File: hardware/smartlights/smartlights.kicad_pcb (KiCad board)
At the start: 2 copper layers, 40 x 65 mm, 22 parts, among them J1 Conn_02x20_Odd_Even_MountingP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, J10 Conn_01x02_MountingPin, J11 Conn_01x02_MountingPin, J2 Conn_01x02_MountingPin, J3 Conn_Coaxial_Power, J4 Conn_01x02_MountingPin, J5 Conn_01x04, J6 Conn_01x02_MountingPin, J7 Conn_01x02_MountingPin, J8 Conn_01x02_MountingPin, J9 Conn_01x02_MountingPin, Q1 IRLZ34N, Q2 IRLZ34N, Q3 IRLZ34N, Q4 IRLZ34N, Q5 IRLZ34N, Q6 IRLZ34N, U1 LM2596T-5

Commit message: Neaten up labels, GND area
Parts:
- renumbered J2 to J1, J3 to J10, J1 to J11, J5 to J2, J6 to J3, J9 to J5, J8 to J6, J11 to J8, J10 to J9
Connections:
- J5 pad 2: Net-(J1-Pad20) -> GND
- J6 pad 2: Net-(J1-Pad20) -> GND
- J7 pad 2: Net-(J1-Pad20) -> GND
- J8 pad 2: Net-(J1-Pad20) -> GND
- J9 pad 2: Net-(J1-Pad20) -> GND
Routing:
- net Net-(J1-Pad20): track 39.5 -> 0.00 mm
- net Net-(J1-Pad22): track 0.00 -> 6.51 mm
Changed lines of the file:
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@@
   (general
     (thickness 1.6)
-    (drawings 14)
-    (tracks 139)
+    (drawings 17)
+    (tracks 132)
     (zones 0)
     (modules 22)
@@
     (descr "Through hole straight pin header, 1x02, 2.54mm pitch, single row")
     (tags "Through hole pin header THT 1x02 2.54mm single row")
-    (fp_text reference J11 (at 0 -2.33 90) (layer F.SilkS)
+    (fp_text reference J8 (at 2.54 2.54 180) (layer F.SilkS)
       (effects (font (size 1 1) (thickness 0.15)))
     )
@@
     (fp_line (start -0.635 -1.27) (end 1.27 -1.27) (layer F.Fab) (width 0.1))
     (pad 2 thru_hole oval (at 0 2.54 90) (size 1.7 1.7) (drill 1) (layers *.Cu *.Mask)
-      (net 20 "Net-(J1-Pad20)"))
+      (net 1 GND))
     (pad 1 thru_hole rect (at 0 0 90) (size 1.7 1.7) (drill 1) (layers *.Cu *.Mask)
       (net 17 "Net-(J1-Pad24)"))
@@
     (descr "Through hole straight pin header, 1x02, 2.54mm pitch, single row")
     (tags "Through hole pin header THT 1x02 2.54mm single row")
-    (fp_text reference J10 (at 0 -2.33 90) (layer F.SilkS)
+    (fp_text reference J9 (at 2.54 2.54 180) (layer F.SilkS)
       (effects (font (size 1 1) (thickness 0.15)))
     )
@@
     (fp_line (start -0.635 -1.27) (end 1.27 -1.27) (layer F.Fab) (width 0.1))
     (pad 2 thru_hole oval (at 0 2.54 90) (size 1.7 1.7) (drill 1) (layers *.Cu *.Mask)
-      (net 20 "Net-(J1-Pad20)"))
+      (net 1 GND))
     (pad 1 thru_hole rect (at 0 0 90) (size 1.7 1.7) (drill 1) (layers *.Cu *.Mask)
       (net 16 "Net-(J1-Pad26)"))
@@
     (descr "Through hole straight pin header, 1x02, 2.54mm pitch, single row")
     (tags "Through hole pin header THT 1x02 2.54mm single row")
-    (fp_text reference J9 (at 0 -2.33 90) (layer F.SilkS)
+    (fp_text reference J5 (at 2.54 2.54 180) (layer F.SilkS)
       (effects (font (size 1 1) (thickness 0.15)))
     )
@@
     (fp_line (start -0.635 -1.27) (end 1.27 -1.27) (layer F.Fab) (width 0.1))
     (pad 2 thru_hole oval (at 0 2.54 90) (size 1.7 1.7) (drill 1) (layers *.Cu *.Mask)
-      (net 20 "Net-(J1-Pad20)"))
+      (net 1 GND))
     (pad 1 thru_hole rect (at 0 0 90) (size 1.7 1.7) (drill 1) (layers *.Cu *.Mask)
       (net 23 "Net-(J1-Pad16)"))
@@
     (descr "Through hole straight pin header, 1x02, 2.54mm pitch, single row")
     (tags "Through hole pin header THT 1x02 2.54mm single row")
-    (fp_text reference J8 (at 0 -2.33 90) (layer F.SilkS)
+    (fp_text reference J6 (at 2.54 2.54 180) (layer F.SilkS)
       (effects (font (size 1 1) (thickness 0.15)))
     )
@@
     (fp_line (start -0.635 -1.27) (end 1.27 -1.27) (layer F.Fab) (width 0.1))
     (pad 2 thru_hole oval (at 0 2.54 90) (size 1.7 1.7) (drill 1) (layers *.Cu *.Mask)
-      (net 20 "Net-(J1-Pad20)"))
+      (net 1 GND))
     (pad 1 thru_hole rect (at 0 0 90) (size 1.7 1.7) (drill 1) (layers *.Cu *.Mask)
       (net 21 "Net-(J1-Pad18)"))
@@
     (descr "Through hole straight pin header, 1x02, 2.54mm pitch, single row")
     (tags "Through hole pin header THT 1x02 2.54mm single row")
-    (fp_text reference J7 (at 0 -2.33 90) (layer F.SilkS)
+    (fp_text reference J7 (at 2.54 2.54 180) (layer F.SilkS)
       (effects (font (size 1 1) (thickness 0.15)))
     )
@@
     (fp_line (start -0.635 -1.27) (end 1.27 -1.27) (layer F.Fab) (width 0.1))
     (pad 2 thru_hole oval (at 0 2.54 90) (size 1.7 1.7) (drill 1) (layers *.Cu *.Mask)
-      (net 20 "Net-(J1-Pad20)"))
+      (net 1 GND))
     (pad 1 thru_hole rect (at 0 0 90) (size 1.7 1.7) (drill 1) (layers *.Cu *.Mask)
       (net 19 "Net-(J1-Pad22)"))
@@
     (descr "TO-220-3, Vertical, RM 2.54mm, see https://www.vishay.com/docs/66542/to-220-1.pdf")
     (tags "TO-220-3 Vertical RM 2.54mm")
-    (fp_text reference Q5 (at 2 2.5 90) (layer F.SilkS)
+    (fp_text reference Q5 (at 2 2.5 180) (layer F.SilkS)
       (effects (font (size 1 1) (thickness 0.15)))
     )
@@
     (descr "Through hole straight pin header, 1x02, 2.54mm pitch, single row")
     (tags "Through hole pin header THT 1x02 2.54mm single row")
-    (fp_text reference J6 (at 0 -2.33) (layer F.SilkS)
+    (fp_text reference J3 (at 0 -2.33) (layer F.SilkS)
       (effects (font (size 1 1) (thickness 0.15)))
     )
@@
     (descr "Through hole straight pin header, 1x04, 2.54mm pitch, single row")
     (tags "Through hole pin header THT 1x04 2.54mm single row")
-    (fp_text reference J5 (at 0 -2.33) (layer F.SilkS)
+    (fp_text reference J2 (at 0 -2.33) (layer F.SilkS)
       (effects (font (size 1 1) (thickness 0.15)))
     )
@@
     (descr "Diode, DO-201AD series, Axial, Horizontal, pin pitch=15.24mm, , length*diameter=9.5*5.2mm^2, , http://www.diodes.com/_files/packages/DO-201AD.pdf")
     (tags "Diode DO-201AD series Axial Horizontal pin pitch 15.24mm  length 9.5mm diameter 5.2mm")
-    (fp_text reference D1 (at 14 2.5 90) (layer F.SilkS)
+    (fp_text reference D1 (at 13.65 3.19 180) (layer F.SilkS)
       (effects (font (size 1 1) (thickness 0.15)))
     )
@@
       (effects (font (size 1 1) (thickness 0.15)))
     )
-    (fp_text user K (at 0.5 3 90) (layer F.SilkS)
+    (fp_text user K (at 0.5 3 180) (layer F.SilkS)
       (effects (font (size 1 1) (thickness 0.15)))
     )
@@
     (descr "TO-220-5, Vertical, RM 1.7mm, Pentawatt, Multiwatt-5, staggered type-1, see http://www.analog.com/media/en/package-pcb-resources/package/pkg_pdf/ltc-legacy-to-220/to-220_5_05-08-1421.pdf?domain=www.linear.com, https://www.diodes.com/assets/Package-Files/TO220-5.pdf")
     (tags "TO-220-5 Vertical RM 1.7mm Pentawatt Multiwatt-5 staggered type-1")
-    (fp_text reference U1 (at 3.4 -9.32 90) (layer F.SilkS)
+    (fp_text reference U1 (at 9.84 -7.42 180) (layer F.SilkS)
       (effects (font (size 1 1) (thickness 0.15)))
     )
@@
     (descr "DC Barrel Jack")
     (tags "Power Jack")
-    (fp_text reference J3 (at -8.45 5.75 90) (layer F.SilkS)
+    (fp_text reference J10 (at -7.88 6.59 180) (layer F.SilkS)
       (effects (font (size 1 1) (thickness 0.15)))
     )
@@
     (descr "Through hole straight pin header, 1x02, 2.54mm pitch, single row")
     (tags "Through hole pin header THT 1x02 2.54mm single row")
-    (fp_text reference J2 (at 0 -2.33) (layer F.SilkS)
+    (fp_text reference J1 (at 0 -2.33) (layer F.SilkS)
       (effects (font (size 1 1) (thickness 0.15)))
     )
@@
     (descr "Through hole straight socket strip, 2x20, 2.54mm pitch, double cols (from Kicad 4.0.7), script generated")
     (tags "Through hole socket strip THT 2x20 2.54mm double row")
-    (fp_text reference J1 (at -1.27 2.77) (layer B.SilkS)
+    (fp_text reference J11 (at 1.23 2.77) (layer B.SilkS)
       (effects (font (size 1 1) (thickness 0.15)) (justify mirror))
     )
@@
     )
   )
+  (gr_line (start 130 68) (end 130 127) (layer B.SilkS) (width 0.12))
+  (gr_arc (start 127 68) (end 130 68) (angle -90) (layer B.SilkS) (width 0.12))
+  (gr_arc (start 127 127) (end 127 130) (angle -90) (layer B.SilkS) (width 0.12))
   (gr_text "rev. 2.1" (at 108.5 128) (layer F.SilkS)
     (effects (font (size 1 1) (thickness 0.15)))
   )
-  (gr_text github.com/mrwonko/smartlights (at 104 87 270) (layer B.SilkS)
+  (gr_text github.com/mrwonko/smartlights (at 138 97 90) (layer B.SilkS)
     (effects (font (size 1 1) (thickness 0.15)) (justify mirror))
   )
@@
   (segment (start 133.35 103.04) (end 131.62 101.31) (width 0.25) (layer F.Cu) (net 17))
   (segment (start 133.35 104.14) (end 133.35 103.04) (width 0.25) (layer F.Cu) (net 17))
-  (segment (start 134.664999 95.294999) (end 135.040001 95.670001) (width 0.25) (layer F.Cu) (net 20))
-  (segment (start 135.040001 95.670001) (end 135.89 96.52) (width 0.25) (layer F.Cu) (net 20))
-  (segment (start 129.907082 95.294999) (end 134.664999 95.294999) (width 0.25) (layer F.Cu) (net 20))
-  (segment (start 128.972081 96.23) (end 129.907082 95.294999) (width 0.25) (layer F.Cu) (net 20))
-  (segment (start 127.77 96.23) (end 128.972081 96.23) (width 0.25) (layer F.Cu) (net 20))
-  (segment (start 135.89 81.28) (end 135.89 88.9) (width 0.25) (layer F.Cu) (net 20))
-  (segment (start 135.89 88.9) (end 135.89 96.52) (width 0.25) (layer F.Cu) (net 20))
-  (segment (start 135.89 96.52) (end 135.89 104.14) (width 0.25) (layer F.Cu) (net 20))
-  (segment (start 135.89 104.14) (end 135.89 111.76) (width 0.25) (layer F.Cu) (net 20))
+  (segment (start 130.02 96.52) (end 127.77 98.77) (width 0.25) (layer F.Cu) (net 19))
+  (segment (start 133.35 96.52) (end 130.02 96.52) (width 0.25) (layer F.Cu) (net 19))
   (segment (start 132.56 88.9) (end 133.35 88.9) (width 0.25) (layer F.Cu) (net 21))
   (segment (start 127.77 93.69) (end 132.56 88.9) (width 0.25) (layer F.Cu) (net 21))
@@
     (polygon
       (pts
-        (xy 124 102.5) (xy 116 110.5) (xy 116 115) (xy 111.5 119.5) (xy 106 119.5)
-        (xy 106 102.5) (xy 101 102.5) (xy 101 71.5) (xy 106.5 71.5) (xy 106.5 66)
-        (xy 124 66)
+        (xy 140 130) (xy 100 130) (xy 100 65) (xy 140 65)
       )
     )

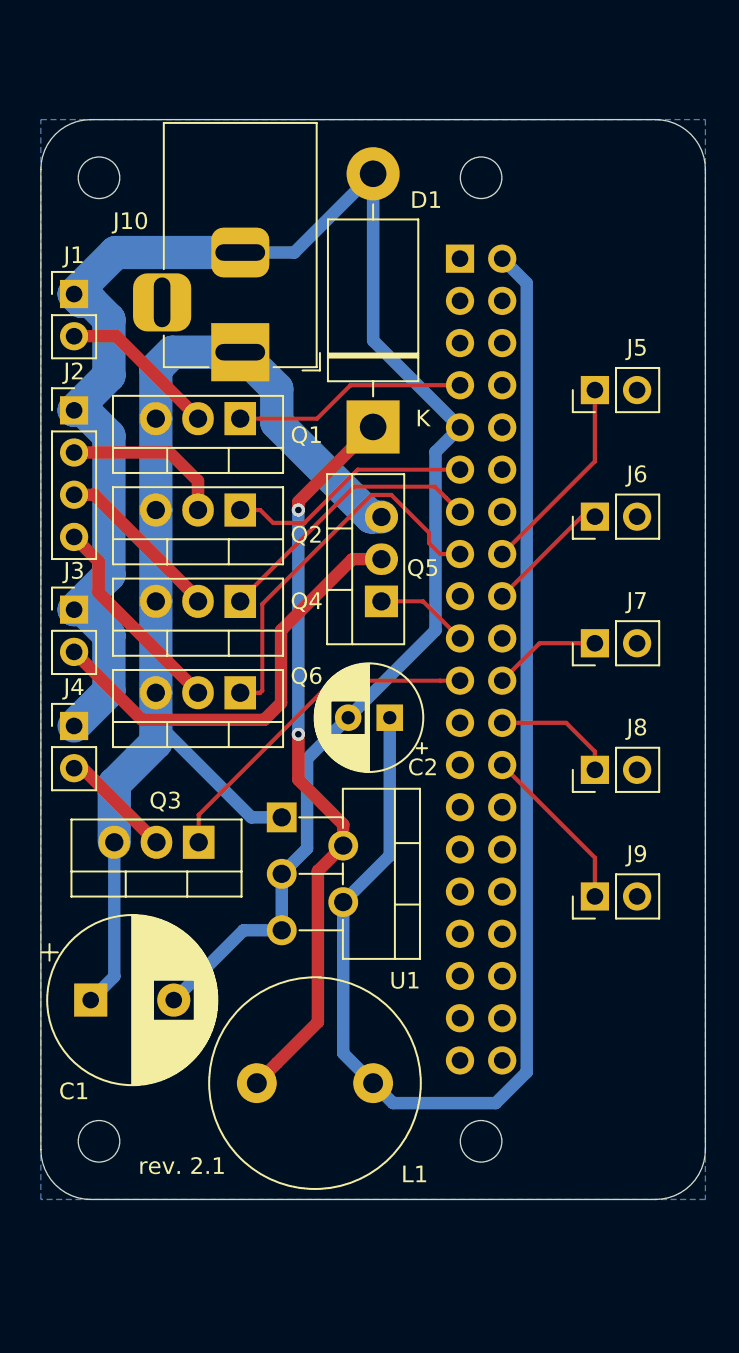
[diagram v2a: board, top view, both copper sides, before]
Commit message: PCB: Use RasPi footprint, reduce GND area around jacks
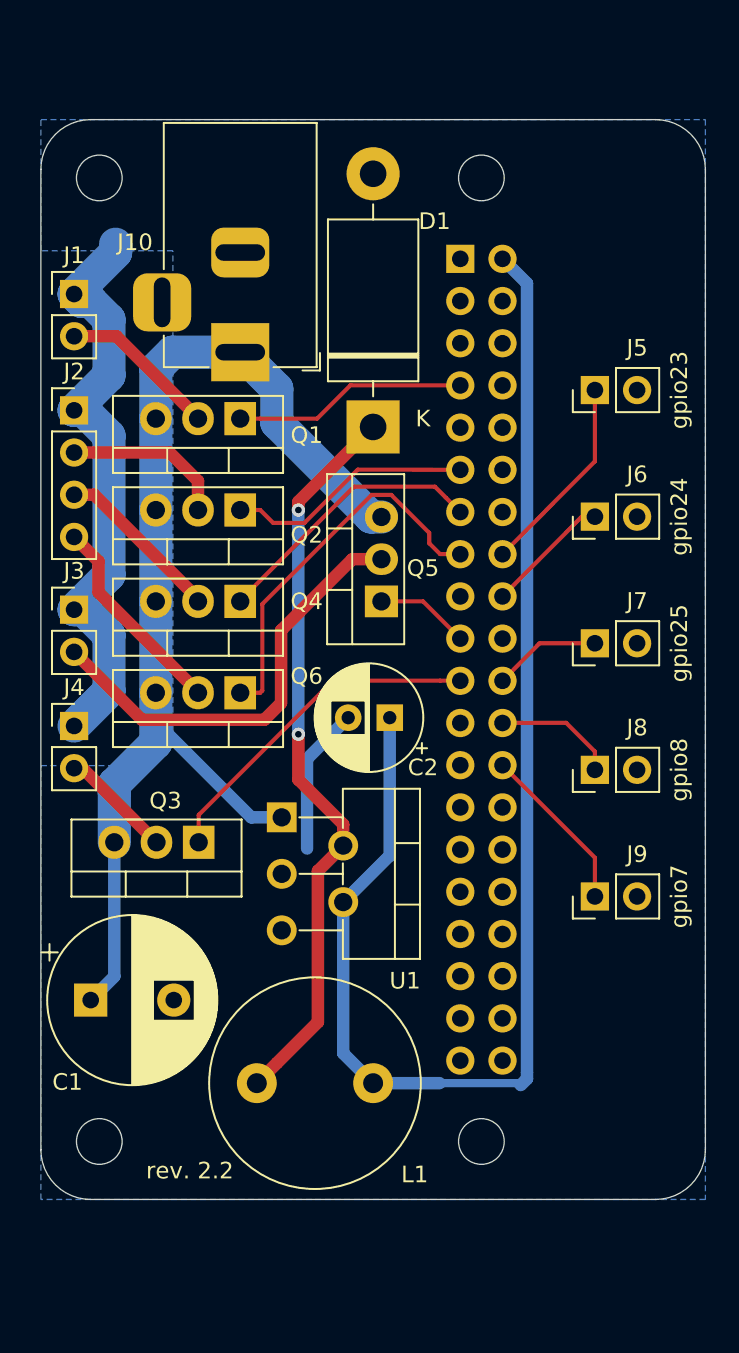
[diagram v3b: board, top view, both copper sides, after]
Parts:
- J11: value Conn_02x20_Odd_Even_MountingPin -> Raspberry_Pi_2_3; footprint Connector_PinSocket_2.54mm:PinSocket_2x20_P2.54mm_Vertical -> Module:Raspberry_Pi_Zero_Socketed_THT_FaceDown_MountingHoles
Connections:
- net /Data_19 renamed pin19
- net /Data_21 renamed pin21
- net /Data_7 renamed pin7
- net /Data_B renamed pin15
- net /Data_G renamed pin13
- net /Data_R renamed pin11
- net /PWR,21 renamed /PWR_21
- net Net-(J11-Pad16) renamed pin16
- net Net-(J11-Pad18) renamed pin18
- net Net-(J11-Pad22) renamed pin22
- net Net-(J11-Pad24) renamed pin24
- net Net-(J11-Pad26) renamed pin26
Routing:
- net GND: track 113.6 -> 45.2 mm
- net 5V: track 84.0 -> 83.3 mm
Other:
- outline, holes or cut-outs redrawn
- board text added: "gpio23"
- board text added: "gpio24"
- board text added: "gpio25"
- board text added: "gpio7"
- board text added: "gpio8"
- board text added: "rev. 2.2"
- board text removed: "rev. 2.1"

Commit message: Add power button and connect more 5V/GND pins. For beaut.
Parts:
- added SW1: SW_Push, Button_Switch_THT:SW_PUSH_6mm, F.Cu at (132.0, 75.0)
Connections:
- J11 pad 25: Net-(J11-Pad25) -> GND
- J11 pad 39: Net-(J11-Pad39) -> GND
- J11 pad 4: Net-(J11-Pad4) -> 5V
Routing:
- net Net-(J11-Pad5): track 0.00 -> 14.7 mm
- net 5V: track 83.3 -> 85.7 mm
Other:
- board text added: "rev. 2.3"
- board text removed: "rev. 2.2"

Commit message: Move back print to front to reduce manufacturing costs
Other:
- board text added: "rev. 2.4"
- board text removed: "rev. 2.3"
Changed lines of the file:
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@@
     (descr "Raspberry Pi Zero using through hole straight pin socket, 2x20, 2.54mm pitch, https://www.raspberrypi.org/documentation/hardware/raspberrypi/mechanical/rpi_MECH_Zero_1p2.pdf")
     (tags "raspberry pi zero through hole")
-    (fp_text reference J11 (at -6.27 -24.13 -90) (layer B.SilkS)
-      (effects (font (size 1 1) (thickness 0.15)) (justify mirror))
+    (fp_text reference J11 (at -5.0026 -4.6194 90) (layer F.SilkS)
+      (effects (font (size 1 1) (thickness 0.15)))
     )
     (fp_text value Raspberry_Pi_2_3 (at 10.23 -24.13 90) (layer B.Fab)
@@
     (effects (font (size 1 1) (thickness 0.15)))
   )
-  (gr_text "rev. 2.3" (at 108.966 128.27) (layer F.SilkS)
+  (gr_text "rev. 2.4" (at 108.966 128.27) (layer F.SilkS)
     (effects (font (size 1 1) (thickness 0.15)))
   )
-  (gr_text github.com/mrwonko/smartlights (at 138 97 90) (layer B.SilkS)
-    (effects (font (size 1 1) (thickness 0.15)) (justify mirror))
+  (gr_text github.com/mrwonko/smartlights (at 130.25 96.75 90) (layer F.SilkS)
+    (effects (font (size 1 1) (thickness 0.15)))
   )
   (gr_line (start 140 68) (end 140 127) (layer Edge.Cuts) (width 0.05))

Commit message: Fix wrong voltage on transistors
Also, the RGB Strip has shared 12V, not GND.
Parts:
- moved J2 7.62 mm to (102.0, 90.1), turned to 180 degrees
- moved J1 2.54 mm to (102.0, 78.0), turned to 180 degrees
- moved J3 2.54 mm to (102.0, 97.0), turned to 180 degrees
- moved J4 2.54 mm to (102.0, 104.0), turned to 180 degrees
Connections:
- J1 pad 1: GND -> /PWR_7
- J1 pad 2: /PWR_7 -> 12V
- J2 pad 1: GND -> /GND_R
- J2 pad 2: /PWR_R -> /GND_G
- J2 pad 3: /PWR_G -> /GND_B
- J2 pad 4: /PWR_B -> 12V
- J3 pad 1: GND -> /PWR_19
- J3 pad 2: /PWR_19 -> 12V
- J4 pad 1: GND -> /PWR_21
- J4 pad 2: /PWR_21 -> 12V
- Q1 pad 3: 12V -> GND
- Q2 pad 2: /PWR_R -> /GND_B
- Q2 pad 3: 12V -> GND
- Q3 pad 3: 12V -> GND
- Q4 pad 2: /PWR_G -> /GND_G
- Q4 pad 3: 12V -> GND
- Q5 pad 3: 12V -> GND
- Q6 pad 2: /PWR_B -> /GND_R
- Q6 pad 3: 12V -> GND
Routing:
- net 12V: track 70.6 -> 32.2 mm
- net /PWR_B: track 12.5 -> 0.00 mm
- net /GND_R: track 0.00 -> 12.5 mm
- net /PWR_G: track 10.2 -> 0.00 mm
- net /GND_G: track 0.00 -> 10.2 mm
- net /PWR_R: track 9.92 -> 0.00 mm
- net /GND_B: track 0.00 -> 9.92 mm
- net GND: track 45.2 -> 37.8 mm
